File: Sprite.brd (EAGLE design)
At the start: 35 x 35 mm, 28 parts, among them P1 SPRITE_PIN, P2 SPRITE_PIN, U1 CC430F5137, U2 LSM9DS1, X1 TCXO_7Z

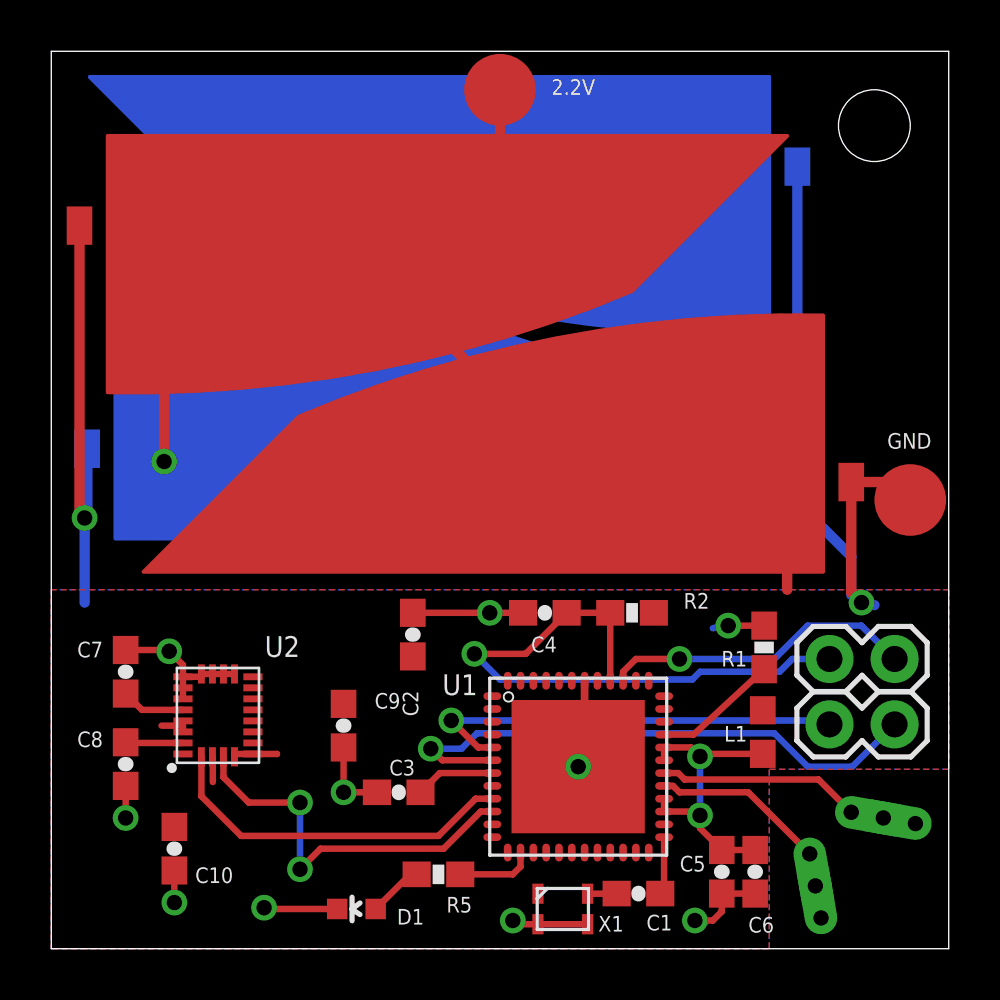
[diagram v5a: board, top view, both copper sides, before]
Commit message: Swapped pins
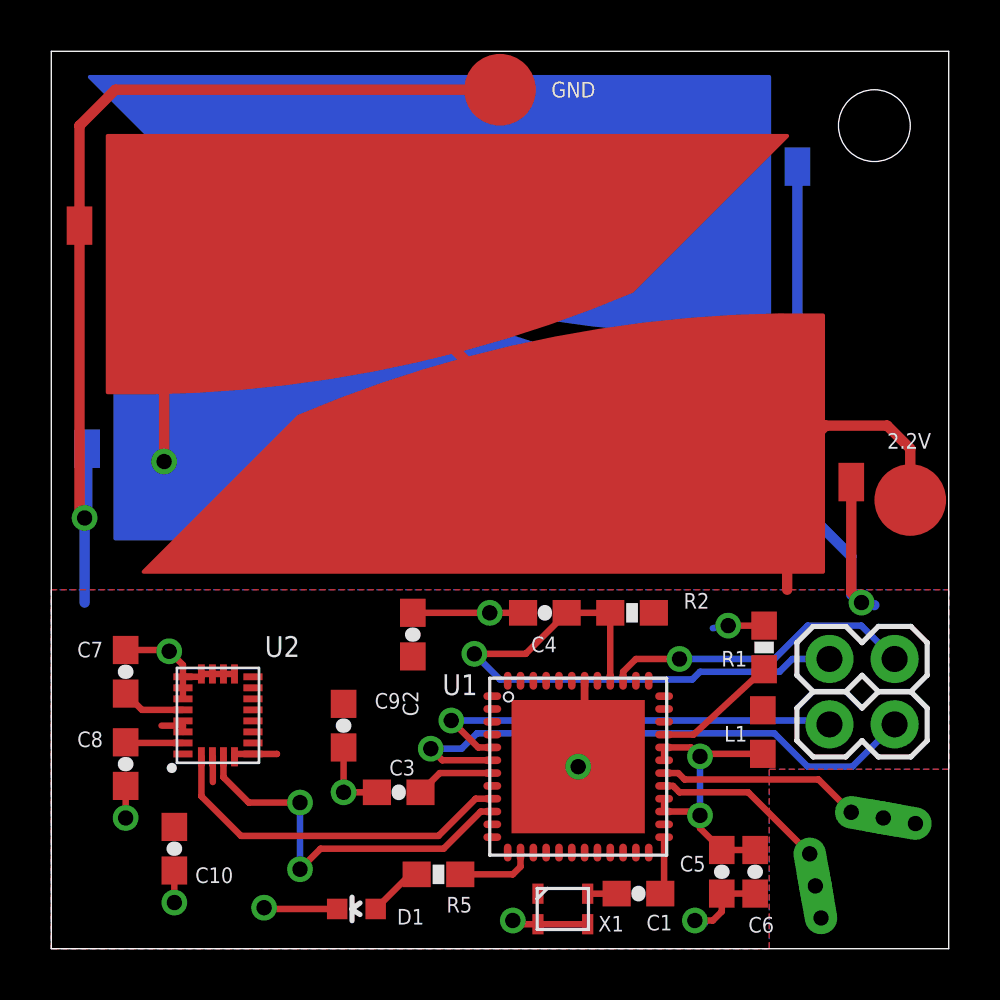
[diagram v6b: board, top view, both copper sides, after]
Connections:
- net GND: now also P1.PIN; no longer P2.PIN
- net VCC: now also P2.PIN; no longer P1.PIN
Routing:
- net GND: track 75.0 -> 93.2 mm
- net VCC: track 81.5 -> 86.6 mm
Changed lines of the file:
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@@
 <rectangle x1="6.46430625" y1="8.135621875" x2="6.4998625" y2="8.140696875" layer="201" rot="R180"/>
 <text x="11.775434375" y="2.794003125" size="0.635" layer="201" font="vector" rot="MR0">Sprite v2.6</text>
-<text x="32.6" y="19.5" size="0.6096" layer="25">GND</text>
-<text x="19.5" y="33.3" size="0.6096" layer="25">2.2V</text>
+<text x="19.5" y="33.2" size="0.6096" layer="25">GND</text>
+<text x="32.6" y="19.5" size="0.6096" layer="25">2.2V</text>
 </plain>
 <attributes>
@@
 <wire x1="6.285" y1="7.485" x2="6.3" y2="7.485" width="0.254" layer="1"/>
 <wire x1="6.3" y1="7.485" x2="6.3" y2="6.5" width="0.254" layer="1"/>
-<contactref element="P1" pad="PIN"/>
 <wire x1="20.2" y1="18.9" x2="13.7" y2="25.4" width="0.4064" layer="1"/>
-<wire x1="17.5" y1="33.5" x2="17.5" y2="30.8" width="0.4064" layer="1"/>
 <wire x1="17.5" y1="30.8" x2="13.4" y2="26.7" width="0.4064" layer="1"/>
 <wire x1="13.7" y1="25.4" x2="13.7" y2="26.4" width="0.4064" layer="1"/>
 <wire x1="13.7" y1="26.4" x2="13.4" y2="26.7" width="0.4064" layer="1"/>
+<contactref element="P2" pad="PIN"/>
+<wire x1="33.5" y1="17.5" x2="33.5" y2="19.5" width="0.4064" layer="1"/>
+<wire x1="33.5" y1="19.5" x2="32.6" y2="20.4" width="0.4064" layer="1"/>
+<wire x1="32.6" y1="20.4" x2="30.2" y2="20.4" width="0.4064" layer="1"/>
+<wire x1="30.2" y1="20.4" x2="28.7" y2="18.9" width="0.4064" layer="1"/>
 </signal>
 <signal name="GND">
@@
 <wire x1="4.8" y1="1.8" x2="4.8" y2="1.7" width="0.254" layer="16"/>
 <wire x1="4.8" y1="1.7" x2="4.9" y2="1.6" width="0.254" layer="16"/>
-<contactref element="P2" pad="PIN"/>
-<wire x1="31.2" y1="18.2" x2="32.8" y2="18.2" width="0.4064" layer="1"/>
-<wire x1="32.8" y1="18.2" x2="33.5" y2="17.5" width="0.4064" layer="1"/>
 <wire x1="14.1" y1="13.1" x2="17.1" y2="13.1" width="0.254" layer="1"/>
+<contactref element="P1" pad="PIN"/>
+<wire x1="17.5" y1="33.5" x2="2.5" y2="33.5" width="0.4064" layer="1"/>
+<wire x1="2.5" y1="33.5" x2="1.1" y2="32.1" width="0.4064" layer="1"/>
+<wire x1="1.1" y1="32.1" x2="1.1" y2="28.2" width="0.4064" layer="1"/>
 </signal>
 <signal name="N$3">
